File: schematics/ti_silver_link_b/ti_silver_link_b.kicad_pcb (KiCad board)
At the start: 2 copper layers, 65.3 x 18.2 mm, 42 parts, among them P1 Conn_1x5, U1 24LC64, U2 TPS71533__SC70, U3 TUSB3410, U4 IMH8A, Y1 12MHz

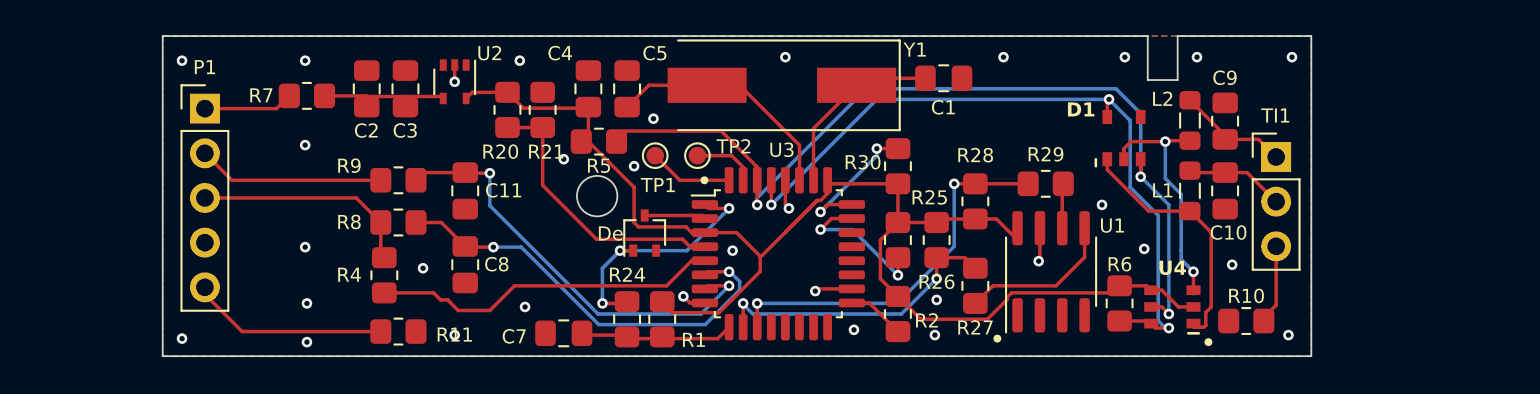
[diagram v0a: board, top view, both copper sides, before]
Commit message: Update and fix "B" schematic's footprints and layout
Wrong pinout was used in U4 and D1
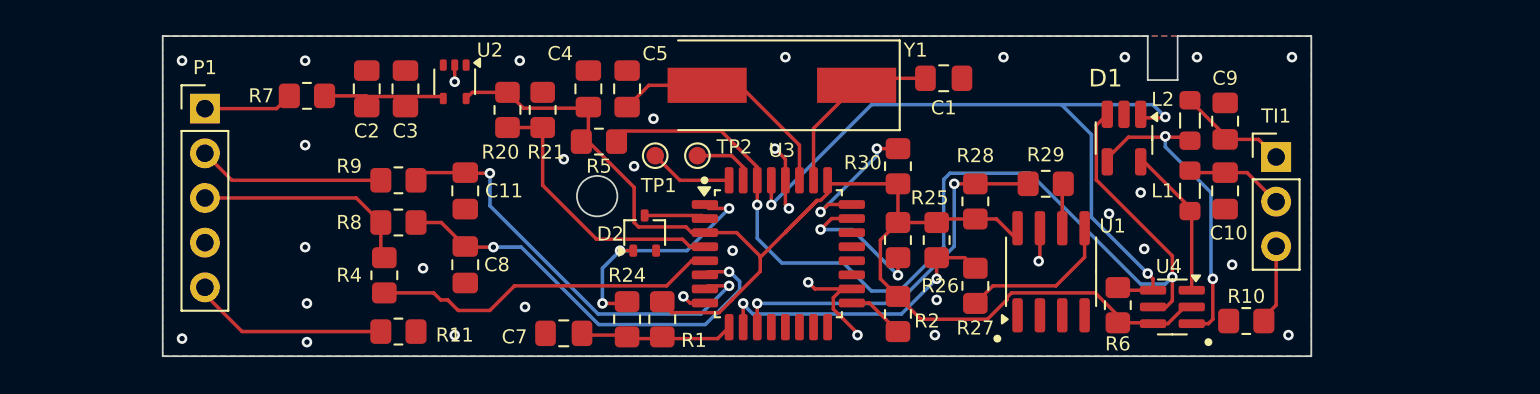
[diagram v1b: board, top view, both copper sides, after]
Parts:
- D1: footprint Package_TO_SOT_SMD:SOT-753 -> ti_graph_link_library:SOT-25_HandSoldering_clockwise_pin_numbering
- U4: footprint Package_TO_SOT_SMD:SOT-457 -> Package_TO_SOT_SMD:ROHM_SOT-457_ClockwisePinNumbering
- moved R6 0.14 mm to (154.3, 115.3), turned to -90 degrees
- turned D1 to -90 degrees
- turned U4 to -90 degrees
- renumbered De to D2
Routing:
- net MCU_TIP: track 50.2 -> 59.1 mm, vias 3 -> 2
- net GND: track 8.04 -> 14.6 mm, vias 32 -> 34
- net Net-(U4A-C1): track 13.7 -> 19.5 mm
- net Net-(U4B-C1): track 14.1 -> 8.70 mm
- net MCU_RING: track 41.7 -> 43.9 mm
- net +3V3: track 77.4 -> 78.1 mm

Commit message: Add USB and audio jack connectors to "B" schematic and pcb layout
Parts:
- added J1: USB-B, ti_graph_link_library:USB_B_Logitech_C270_cable_connector, F.Cu at (96.3, 109.2)
- added TI2: Wire, ti_graph_link_library:Jack_2.5mm_with_switch-SMT_Horizontal, F.Cu at (171.7, 109.2)
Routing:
- net Net-(TI1-Pin_3): track 4.62 -> 25.3 mm
- net Net-(J1-Shield): track 11.4 -> 25.0 mm
- net Net-(TI1-Pin_2): track 5.63 -> 15.2 mm
- net Net-(J1-VBUS): track 5.50 -> 10.4 mm
- net Net-(TI1-Pin_1): track 6.54 -> 11.0 mm
- net Net-(J1-D-): track 10.6 -> 14.8 mm
- net GND: track 14.6 -> 18.3 mm, vias 34 -> 41
- net Net-(J1-D+): track 13.1 -> 16.7 mm
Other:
- board size 65.3 x 18.2 mm -> 83.4 x 18.2 mm
